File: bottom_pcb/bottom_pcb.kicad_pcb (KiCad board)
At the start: 2 copper layers, 43.2 x 85 mm, 4 parts

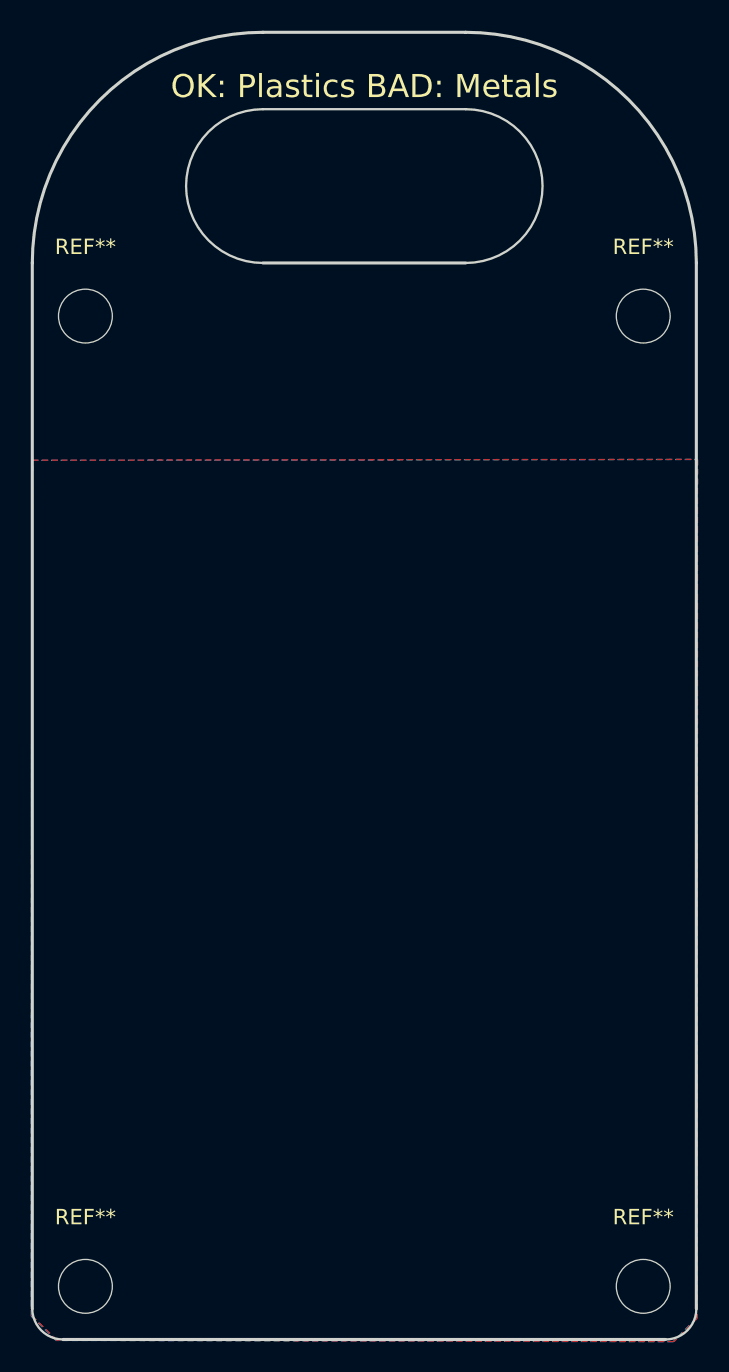
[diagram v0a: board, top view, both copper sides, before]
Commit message: Correct size of bottom pcb
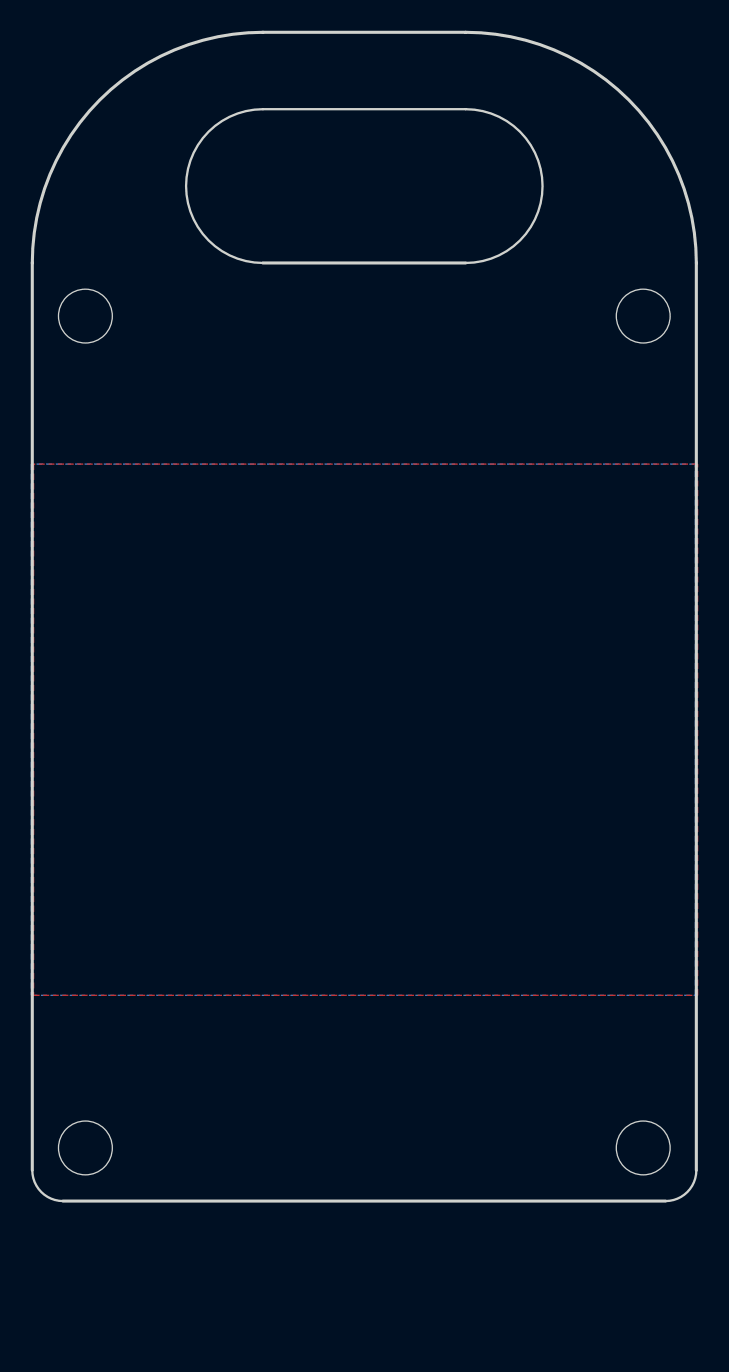
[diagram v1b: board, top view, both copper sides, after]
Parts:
- moved REF** 9.00 mm to (165.8, 107.0)
- moved REF** 9.00 mm to (129.5, 107.0)
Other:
- board size 43.2 x 85 mm -> 43.2 x 76 mm
- board text removed: "OK: Plastics BAD: Metals"
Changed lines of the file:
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@@
   (general
     (thickness 1.6)
-    (drawings 13)
+    (drawings 12)
     (tracks 0)
     (zones 0)
@@
     (tags "mounting hole 3.5mm no annular")
     (attr virtual)
-    (fp_text reference REF** (at 0 -4.5) (layer F.SilkS)
+    (fp_text reference REF** (at 0 -4.5) (layer F.SilkS) hide
       (effects (font (size 1 1) (thickness 0.15)))
     )
@@
     (tags "mounting hole 3.5mm no annular")
     (attr virtual)
-    (fp_text reference REF** (at 0 -4.5) (layer F.SilkS)
+    (fp_text reference REF** (at 0 -4.5) (layer F.SilkS) hide
       (effects (font (size 1 1) (thickness 0.15)))
     )
@@
   )
   (module MountingHole:MountingHole_3.5mm (layer F.Cu)
-    (at 165.77096 115.9514)
+    (at 165.77096 106.9514)
     (descr "Mounting Hole 3.5mm, no annular")
     (tags "mounting hole 3.5mm no annular")
     (attr virtual)
-    (fp_text reference REF** (at 0 -4.5) (layer F.SilkS)
+    (fp_text reference REF** (at 0 -4.5) (layer F.SilkS) hide
       (effects (font (size 1 1) (thickness 0.15)))
     )
@@
   )
   (module MountingHole:MountingHole_3.5mm (layer F.Cu)
-    (at 129.49896 115.9514)
+    (at 129.49896 106.9514)
     (descr "Mounting Hole 3.5mm, no annular")
     (tags "mounting hole 3.5mm no annular")
     (attr virtual)
-    (fp_text reference REF** (at 0 -4.5) (layer F.SilkS)
+    (fp_text reference REF** (at 0 -4.5) (layer F.SilkS) hide
       (effects (font (size 1 1) (thickness 0.15)))
     )
@@
     (pad 1 np_thru_hole circle (at 0 0) (size 3.5 3.5) (drill 3.5) (layers *.Cu *.Mask))
   )
-  (gr_text "OK: Plastics BAD: Metals" (at 147.64004 37.9222) (layer F.SilkS)
-    (effects (font (size 1.5 1.5) (thickness 0.3)))
-  )
   (gr_arc (start 141.04496 49.4054) (end 141.04496 34.4054) (angle -90) (layer Edge.Cuts) (width 0.2))
   (gr_arc (start 154.22496 49.4054) (end 169.22496 49.4054) (angle -90) (layer Edge.Cuts) (width 0.2))
-  (gr_arc (start 167.22496 117.4054) (end 167.22496 119.4054) (angle -90) (layer Edge.Cuts) (width 0.15))
-  (gr_arc (start 128.04496 117.4054) (end 126.04496 117.4054) (angle -90) (layer Edge.Cuts) (width 0.15))
+  (gr_arc (start 167.22496 108.4054) (end 167.22496 110.4054) (angle -90) (layer Edge.Cuts) (width 0.15))
+  (gr_arc (start 128.04496 108.4054) (end 126.04496 108.4054) (angle -90) (layer Edge.Cuts) (width 0.15))
   (gr_arc (start 154.22496 44.4054) (end 154.22496 49.4054) (angle -180) (layer Edge.Cuts) (width 0.15))
   (gr_arc (start 141.04496 44.4054) (end 141.04496 39.4054) (angle -180) (layer Edge.Cuts) (width 0.15))
@@
   (gr_line (start 141.04496 49.4054) (end 154.22496 49.4054) (layer Edge.Cuts) (width 0.2))
   (gr_line (start 154.22496 34.4054) (end 141.04496 34.4054) (layer Edge.Cuts) (width 0.2))
-  (gr_line (start 169.22496 117.4054) (end 169.22496 49.4054) (layer Edge.Cuts) (width 0.2))
-  (gr_line (start 128.04496 119.4054) (end 167.22496 119.4054) (layer Edge.Cuts) (width 0.2))
-  (gr_line (start 126.04496 49.4054) (end 126.04496 117.4054) (layer Edge.Cuts) (width 0.2))
+  (gr_line (start 169.22496 108.4054) (end 169.22496 49.4054) (layer Edge.Cuts) (width 0.2))
+  (gr_line (start 128.04496 110.4054) (end 167.22496 110.4054) (layer Edge.Cuts) (width 0.2))
+  (gr_line (start 126.04496 49.4054) (end 126.04496 108.4054) (layer Edge.Cuts) (width 0.2))
+  (zone (net 0) (net_name "") (layer B.Cu) (hatch edge 0.508)
+    (connect_pads (clearance 0.508))
+    (min_thickness 0.254)
+    (fill yes (arc_segments 16) (thermal_gap 0.508) (thermal_bridge_width 0.508))
+    (polygon
+      (pts
+        (xy 169.164 62.484) (xy 125.984 62.484) (xy 125.984 97.028) (xy 169.164 97.028)
+      )
+    )
+  )
   (zone (net 0) (net_name "") (layer F.Cu) (hatch edge 0.508)
     (connect_pads (clearance 0.508))
@@
     (polygon
       (pts
-        (xy 126.07036 62.23) (xy 169.30624 62.17412) (xy 169.27068 118.03888) (xy 167.77208 119.53748) (xy 127.65024 119.4562)
-        (xy 126.02464 117.87124)
+        (xy 169.310157 62.484) (xy 126.130157 62.484) (xy 126.130157 97.028) (xy 169.310157 97.028)
       )
     )
-  )
-  (zone (net 0) (net_name "") (layer B.Cu) (hatch edge 0.508)
-    (connect_pads (clearance 0.508))
-    (min_thickness 0.254)
-    (fill yes (arc_segments 16) (thermal_gap 0.508) (thermal_bridge_width 0.508))
-    (polygon
-      (pts
-        (xy 126.015145 62.241091) (xy 169.251025 62.185211) (xy 169.215465 118.049971) (xy 167.716865 119.548571) (xy 127.595025 119.467291)
-        (xy 125.969425 117.882331)
-      )
-    )
